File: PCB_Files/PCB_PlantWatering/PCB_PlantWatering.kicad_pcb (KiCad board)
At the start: 4 copper layers, 109.2 x 129.5 mm, 110 parts, among them J1 Battery connection, J1 Connector to PCB2, J10 I2C Pins, J11 I2C Pins, J13 USB_C_Receptacle_USB2.0_16P, J2 AnalogSignals, J2 LED_Strip, J3 32KHZ/SQW, J3 I2C, J4 Power, J4 Solar Panel, J5 Power output, J6 Signal Sockets, J7 Connector to PCB01, J8 I2C, J9 PWR_Output, Q1 MUN5211DW1, SW1 SW_Push, SW2 SW_Push, SW3 SW_Push, SW4 SW_Push, U1 ESP32-DevKitC, U10 DS3231MZ, U11 TP4056-42-ESOP8, U12 AT24CS32-SSHM, U13 MQ-6, U14 MT3608, U2 CP2102N-Axx-xQFN28, U3 XC6220B331MR, U4 BMP280, U5 ADS1115IDGS, U6 ADS1115IDGS, U8 DW01A, U9 FS8205A

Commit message: added readme text
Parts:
- removed D4: TX, LED_SMD:LED_0603_1608Metric
- removed D5: RX, LED_SMD:LED_0603_1608Metric
- removed the H1 at (53.7, 116.0)
- removed the H2 at (53.5, 42.0)
- removed the H2 at (53.7, 164.5)
- removed the J1 at (135.5, 92.0)
- removed the J1 at (123.2, 144.5)
- removed the J2 at (145.4, 150.6)
- removed the J2 at (136.5, 70.0)
- removed the J3 at (68.0, 41.5)
- removed the J3 at (66.0, 136.1)
- removed the J4 at (122.2, 163.0)
- removed the J4 at (68.0, 91.5)
- added H1: MountingHole, MountingHole:MountingHole_3.2mm_M3, F.Cu at (144.9, 34.2)
- added H1: MountingHole, MountingHole:MountingHole_3.2mm_M3, F.Cu at (43.4, 122.9)
- added H2: MountingHole, MountingHole:MountingHole_3.2mm_M3, F.Cu at (43.4, 171.4)
- added H2: MountingHole, MountingHole:MountingHole_3.2mm_M3, F.Cu at (42.9, 34.2)
- added H4: MountingHole, MountingHole:MountingHole_3.2mm_M3, F.Cu at (144.9, 82.7)
- added J1: Battery connection, Connector_JST:JST_PH_B2B-PH-K_1x02_P2.00mm_Vertical, F.Cu at (112.9, 151.4)
- added J1: Connector to PCB2, Connector_PinSocket_2.00mm:PinSocket_1x06_P2.00mm_Vertical, F.Cu at (124.9, 84.2)
- added J2: LED_Strip, Connector_JST:JST_PH_B4B-PH-K_1x04_P2.00mm_Vertical, F.Cu at (127.6, 61.5)
- added J2: AnalogSignals, Connector_PinSocket_2.00mm:PinSocket_1x08_P2.00mm_Vertical, F.Cu at (135.1, 157.5)
- added J3: 32KHZ/SQW, Connector_PinSocket_2.00mm:PinSocket_1x02_P2.00mm_Vertical, F.Cu at (55.6, 143.0)
- added J3: I2C, Connector_PinSocket_2.00mm:PinSocket_1x02_P2.00mm_Vertical, F.Cu at (57.4, 33.7)
- added J4: Solar Panel, Connector_JST:JST_PH_B2B-PH-K_1x02_P2.00mm_Vertical, F.Cu at (111.9, 169.9)
- added J4: Power, Connector_PinSocket_2.00mm:PinSocket_1x02_P2.00mm_Vertical, F.Cu at (57.4, 83.7)
- added R20: 10k, Resistor_SMD:R_1206_3216Metric, F.Cu at (88.1, 128.9)
- added R22: 10k, Resistor_SMD:R_1206_3216Metric, F.Cu at (92.0, 132.4)
- added R23: 100k, Resistor_SMD:R_1206_3216Metric, F.Cu at (95.6, 128.6)
- added RX: RX, LED_SMD:LED_0603_1608Metric, F.Cu at (113.5, 75.0)
- added TX: TX, LED_SMD:LED_0603_1608Metric, F.Cu at (113.5, 77.8)
- added U7: CCS811, Package_LGA:AMS_LGA-10-1EP_2.7x4mm_P0.6mm, F.Cu at (91.5, 127.4)
- J7: value Connector to PCB01 -> Connector to other Board
- R1, R2, R3, R7: footprint Resistor_SMD:R_0603_1608Metric -> Resistor_SMD:R_0805_2012Metric
- moved C7 64.7 mm to (133.1, 60.2), turned to 90 degrees
- moved R39 52.9 mm to (118.0, 35.6), turned to 0 degrees
- moved R40 47.4 mm to (118.0, 38.0)
- moved R10 33.4 mm to (117.4, 77.8)
- moved C3 30.5 mm to (131.9, 66.7)
- moved C5 30.5 mm to (136.0, 66.7)
- moved R6 28.5 mm to (128.9, 79.7), turned to 0 degrees
- moved C1 28.3 mm to (103.1, 76.1), turned to -90 degrees
- moved R7 26.8 mm to (128.8, 77.7), turned to 180 degrees
- moved R38 26.7 mm to (118.0, 40.0), turned to 180 degrees
- moved R11 26.6 mm to (117.3, 74.9)
- moved C4 26.4 mm to (131.9, 64.7)
- moved C6 26.4 mm to (136.0, 64.7)
- moved R24 22.5 mm to (58.9, 39.4), turned to -90 degrees
- moved R21 18.7 mm to (61.5, 39.4), turned to -90 degrees
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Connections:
- R25 pad 1: /Analog12 -> /BUTTONS
- R28 pad 1: /Analog12 -> /BUTTONS
- R39 pad 1: /Analog10 -> /GAS_SENSOR
- R40 pad 2: /Analog10 -> /GAS_SENSOR
- SW1 pad 2: /Analog12 -> /BUTTONS
- U1 pad 10: /LCD_D3 -> /LCD_D2
- U1 pad 11: /LCD_D4 -> /LCD_D6
- U1 pad 12: /LCD_D5 -> /LCD_D7
- U1 pad 13: /LCD_D6 -> /LCD_D0
- U1 pad 15: /LCD_D7 -> /LCD_D1
- U1 pad 26: Net-(J2-Pin_2) -> /LCD_WR
- U1 pad 27: /LCD_D0 -> /LCD_D5
- U1 pad 28: /LCD_D1 -> /LCD_D4
- U1 pad 3: /Analog11 -> /BUTTONS
- U1 pad 4: /Analog12 -> /LCD_WR
- U1 pad 5: /Analog9 -> /GAS_SENSOR
- U1 pad 6: /Analog10 -> /LCD_RS
- U1 pad 7: /LCD_CS -> /LED_STRIP
- U1 pad 8: /LCD_WR -> /LCD_CS
- U1 pad 9: /LCD_D2 -> /LCD_D3
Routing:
- net /GAS_SENSOR: track 0.00 -> 95.8 mm
- net /Analog12: track 63.9 -> 0.00 mm
- net /BUTTONS: track 0.00 -> 56.4 mm
- net /RTS: track 59.3 -> 5.62 mm, vias 2 -> 0
- net Net-(U13-B1): track 69.4 -> 16.6 mm, vias 1 -> 0
- net /LED_STRIP: track 0.00 -> 46.9 mm, vias 0 -> 2
- net Net-(D5-K): track 44.7 -> 1.68 mm
- net /GPIO.0: track 46.6 -> 8.82 mm
- net /GPIO.1: track 40.0 -> 6.58 mm
- net Net-(D4-K): track 35.0 -> 1.67 mm
- net Net-(J2-Pin_2): track 33.2 -> 0.00 mm
- net /LCD_D0: track 13.2 -> 42.7 mm
- net +3.3V: track 659.9 -> 632.8 mm, vias 9 -> 8
- net /DTR: track 33.5 -> 6.56 mm
- net /VBUS_IN: track 185.3 -> 158.5 mm
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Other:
- board size 109.2 x 129.5 mm -> 109.5 x 144.2 mm
- board text added: "PlantWatering PCB01 V1"
- board text removed: "PlantWatering PCB01 V0"

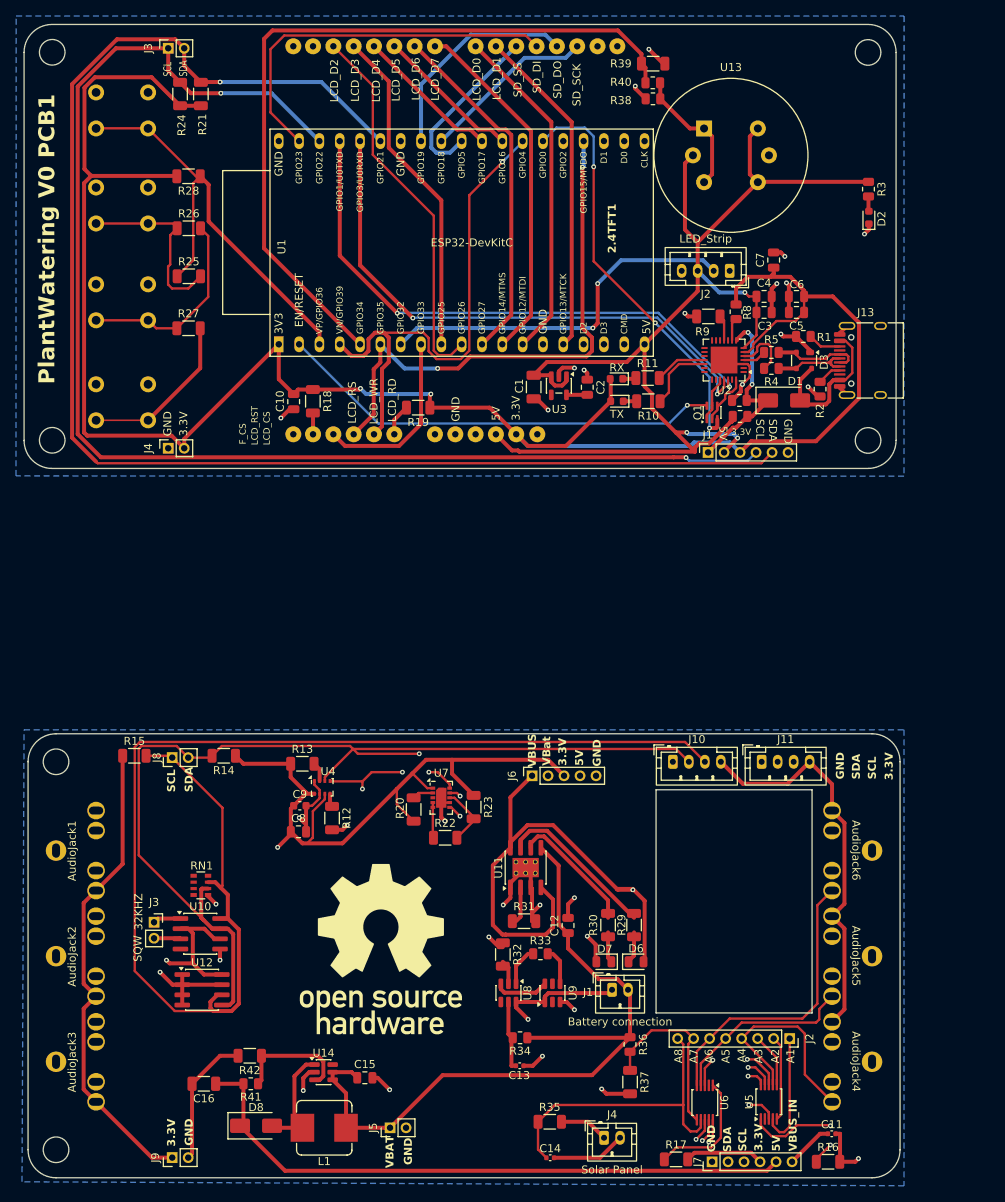
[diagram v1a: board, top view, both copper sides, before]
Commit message: update PDF and added labels to PCB02
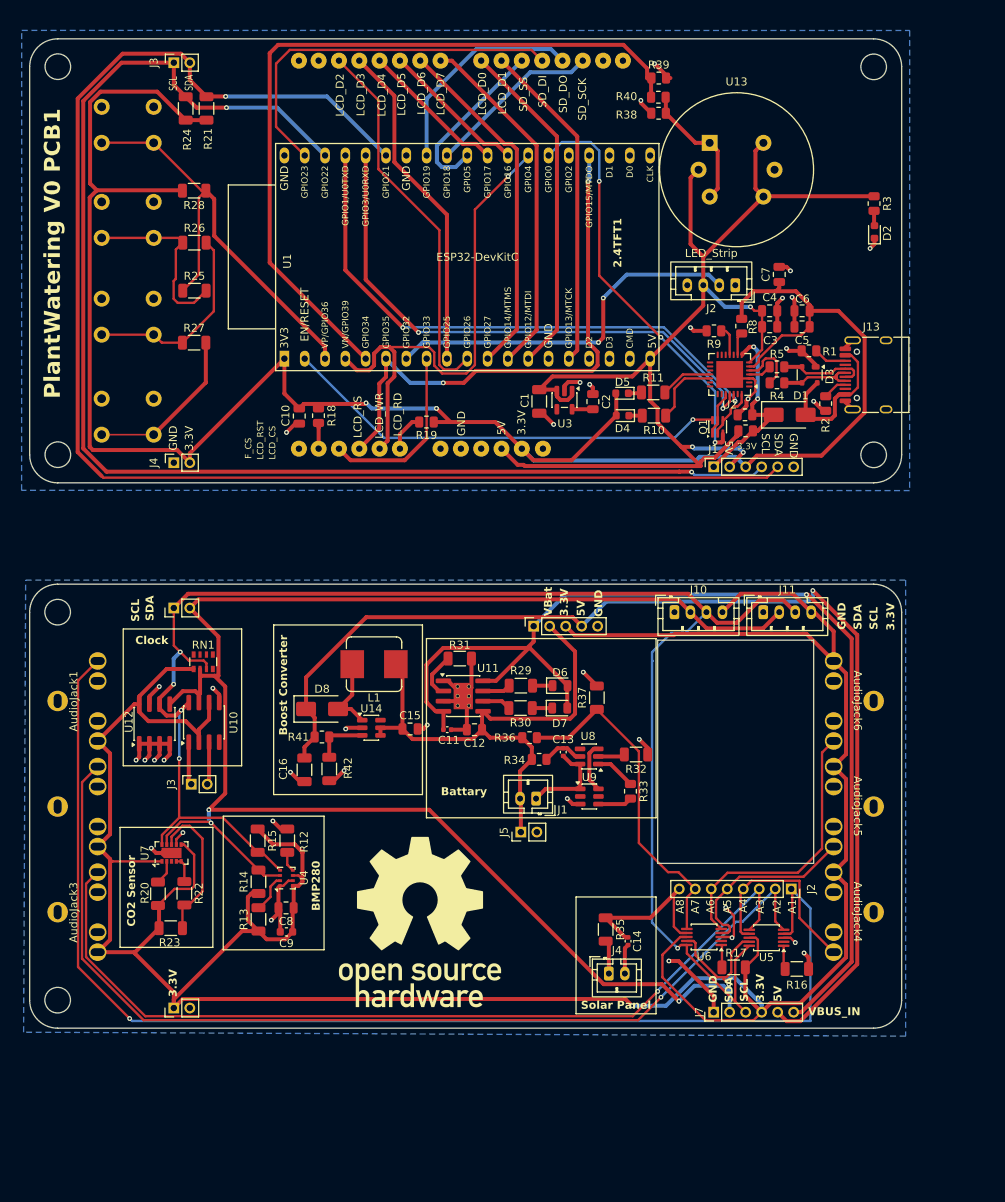
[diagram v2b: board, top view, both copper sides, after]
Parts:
- removed the H1 at (144.9, 34.2)
- removed the H1 at (43.4, 122.9)
- removed the H2 at (43.4, 171.4)
- removed the H2 at (42.9, 34.2)
- removed the J1 at (112.9, 151.4)
- removed the J1 at (124.9, 84.2)
- removed the J2 at (127.6, 61.5)
- removed the J2 at (135.1, 157.5)
- removed the J3 at (55.6, 143.0)
- removed the J3 at (57.4, 33.7)
- removed the J4 at (111.9, 169.9)
- removed the J4 at (57.4, 83.7)
- removed RX: RX, LED_SMD:LED_0603_1608Metric
- removed TX: TX, LED_SMD:LED_0603_1608Metric
- added D4: TX, LED_SMD:LED_0603_1608Metric, F.Cu at (114.2, 79.6)
- added D5: RX, LED_SMD:LED_0603_1608Metric, F.Cu at (114.2, 76.8)
- added H1: MountingHole, MountingHole:MountingHole_3.2mm_M3, F.Cu at (145.6, 36.0)
- added H1: MountingHole, MountingHole:MountingHole_3.2mm_M3, F.Cu at (43.6, 104.2)
- added H2: MountingHole, MountingHole:MountingHole_3.2mm_M3, F.Cu at (43.6, 36.0)
- added H2: MountingHole, MountingHole:MountingHole_3.2mm_M3, F.Cu at (43.6, 152.7)
- added J1: Battery connection, Connector_JST:JST_PH_B2B-PH-K_1x02_P2.00mm_Vertical, F.Cu at (103.4, 127.5)
- added J1: Connector to PCB2, Connector_PinSocket_2.00mm:PinSocket_1x06_P2.00mm_Vertical, F.Cu at (125.6, 86.0)
- added J2: AnalogSignals, Connector_PinSocket_2.00mm:PinSocket_1x08_P2.00mm_Vertical, F.Cu at (135.3, 138.8)
- added J2: LED_Strip, Connector_JST:JST_PH_B4B-PH-K_1x04_P2.00mm_Vertical, F.Cu at (128.3, 63.3)
- added J3: I2C, Connector_PinSocket_2.00mm:PinSocket_1x02_P2.00mm_Vertical, F.Cu at (58.1, 35.5)
- added J3: 32KHZ/SQW, Connector_PinSocket_2.00mm:PinSocket_1x02_P2.00mm_Vertical, F.Cu at (60.3, 125.7)
- added J4: Solar Panel, Connector_JST:JST_PH_B2B-PH-K_1x02_P2.00mm_Vertical, F.Cu at (112.5, 149.4)
- added J4: Power, Connector_PinSocket_2.00mm:PinSocket_1x02_P2.00mm_Vertical, F.Cu at (58.1, 85.5)
- R18, R19, R39, R9: footprint Resistor_SMD:R_1206_3216Metric -> Resistor_SMD:R_0805_2012Metric
- moved C11 69.7 mm to (92.3, 118.9)
- moved L1 58.3 mm to (83.2, 110.7)
- moved D8 52.7 mm to (76.7, 116.3)
- moved R37 48.2 mm to (111.0, 114.9), turned to 90 degrees
- moved R41 44.3 mm to (76.6, 119.8)
- moved C15 44.0 mm to (87.7, 118.8)
- moved U14 43.5 mm to (82.8, 118.7)
- moved C16 41.2 mm to (74.5, 123.9), turned to -90 degrees
- moved R23 40.8 mm to (57.7, 143.7), turned to 0 degrees
- moved J5 40.4 mm to (101.5, 131.7)
- moved R36 40.4 mm to (102.6, 119.9), turned to 0 degrees
- moved C13 39.6 mm to (106.8, 121.7), turned to -90 degrees
- moved R42 37.2 mm to (77.5, 123.8), turned to -90 degrees
- moved D6 35.8 mm to (106.4, 113.4)
- moved R34 34.9 mm to (103.8, 122.6), turned to 0 degrees
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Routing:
- net /SCL: track 462.4 -> 374.1 mm
- net /VBat: track 124.5 -> 68.4 mm
- net /Analog1: track 125.1 -> 157.7 mm, vias 0 -> 1
- net /Analog2: track 105.7 -> 127.0 mm, vias 0 -> 1
- net /Analog7: track 22.7 -> 42.7 mm
- net /Analog8: track 38.7 -> 21.4 mm
- net Net-(U11-~{CHRG}): track 20.1 -> 3.54 mm
- net /Analog3: track 95.1 -> 110.7 mm, vias 0 -> 1
- net /SDA: track 429.2 -> 415.1 mm
- net GND: track 146.2 -> 132.6 mm, vias 30 -> 36
- net +3.3V: track 632.8 -> 619.2 mm, vias 8 -> 3
- net Net-(U5-ADDR): track 15.9 -> 2.98 mm, vias 2 -> 0
- net Net-(U11-~{STDBY}): track 16.1 -> 3.58 mm
- net Net-(U6-ADDR): track 15.1 -> 2.84 mm
- net /S1: track 24.0 -> 11.9 mm, vias 2 -> 0
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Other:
- board size 109.5 x 144.2 mm -> 109 x 123.7 mm
- board text added: "Battary"
- board text added: "Boost Converter"
- board text added: "CO2 Sensor"
- board text added: "Clock"
- board text added: "Solar Panel"
- board text removed: "32KHZ"
- board text removed: "SQW"
- board text removed: "VBAT"
- board text removed: "VBUS"
